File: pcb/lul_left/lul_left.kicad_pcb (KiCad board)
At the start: 2 copper layers, 238.5 x 84.2 mm, 48 parts, among them J1 JST Connector, J2 JST Connector, SW1 SW_Push, SW10 SW_Push, SW11 SW_Push, SW12 SW_Push, SW13 SW_Push, SW14 SW_Push, SW15 SW_Push, SW16 SW_Push, SW17 SW_Push, SW18 SW_Push, SW19 SW_Push, SW2 SW_Push, SW20 SW_Push, SW21 SW_Push, SW22 SW_Push, SW23 SW_Push, SW24 SW_Push, SW25 SW_Push, SW26 SW_Push, SW27 SW_Push, SW28 SW_Push, SW29 SW_Push, SW3 SW_Push, SW30 SW_Push, SW31 SW_Push, SW32 SW_Push, SW33 SW_Push, SW34 SW_Push, SW4 SW_Push, SW5 SW_Push, SW6 SW_Push, SW7 SW_Push, SW8 SW_Push, SW9 SW_Push, U1 nice_nano, U2 nice_nano

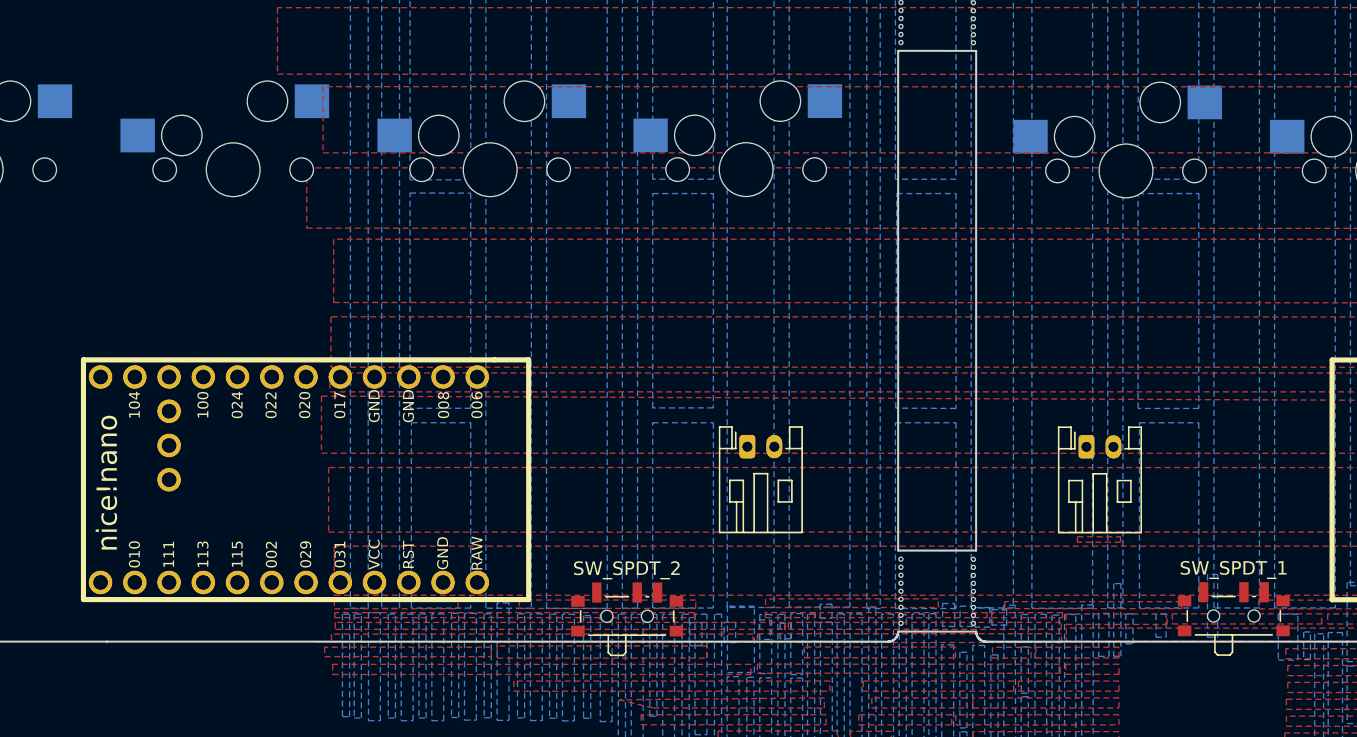
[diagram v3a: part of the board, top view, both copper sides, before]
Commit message: touch up dimensions and positions
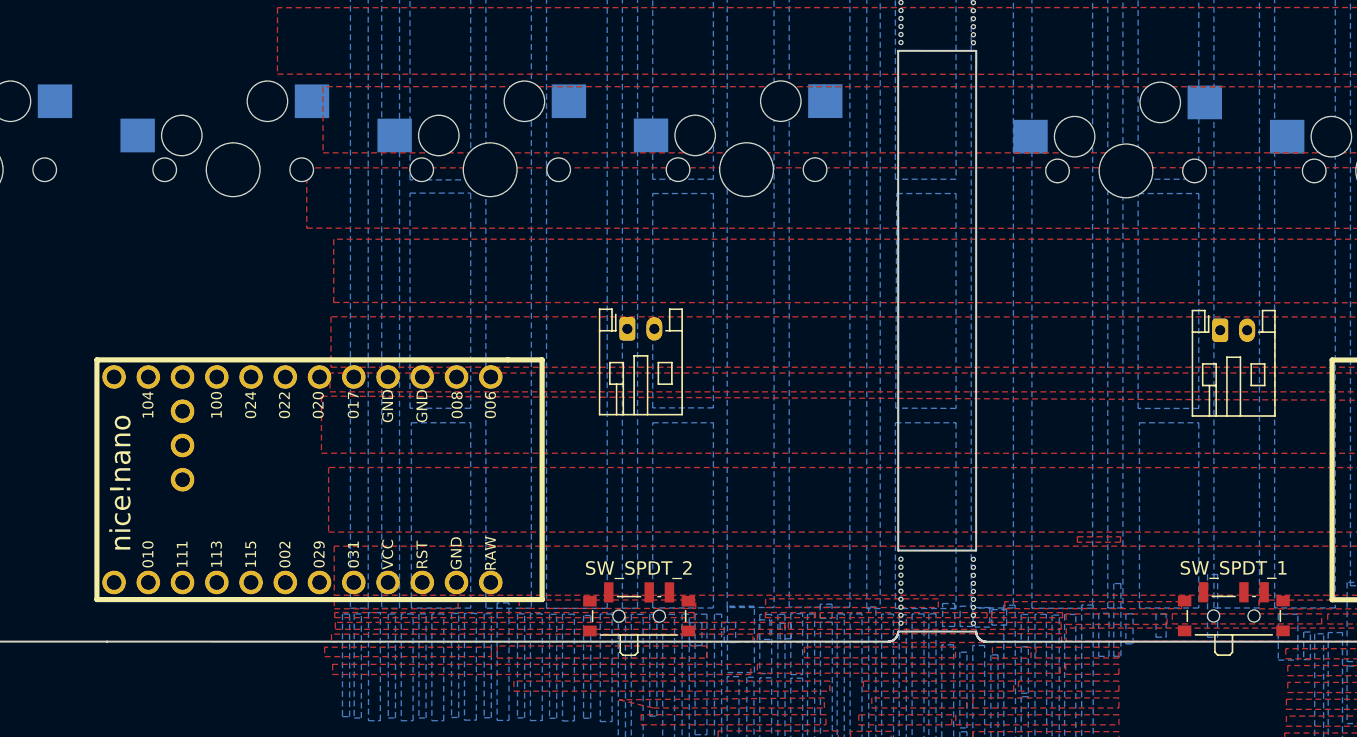
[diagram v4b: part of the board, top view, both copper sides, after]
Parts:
- moved J1 13.2 mm to (163.1, 83.2)
- moved J2 12.5 mm to (119.1, 83.1)
- moved U2 1.00 mm to (95.0, 94.3)
- moved SW_SPDT_2 0.89 mm to (120.0, 104.1)
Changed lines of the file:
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@@
   )
   (footprint "MX_Only:MXOnly-1U-Hotswap" (layer "F.Cu")
-    (at 127.929654 71.267042)
+    (at 127.96 71.27)
     (property "Sheetfile" "lul_left.kicad_sch")
     (property "Sheetname" "")
@@
   )
   (footprint "nice-nano-kicad:nice_nano" (layer "F.Cu")
-    (at 94.019654 94.267042 180)
+    (at 95.019654 94.267042 180)
     (property "Sheetfile" "lul_left.kicad_sch")
     (property "Sheetname" "")
@@
   )
   (footprint "Connector_JST:JST_PH_S2B-PH-K_1x02_P2.00mm_Horizontal" (layer "F.Cu")
-    (at 128.019654 91.817042)
+    (at 119.12 83.08)
     (descr "JST PH series connector, S2B-PH-K (http://www.jst-mfg.com/product/pdf/eng/ePH.pdf), generated with kicad-footprint-generator")
     (tags "connector JST PH top entry")
@@
   )
   (footprint "Button_Switch_SMD:SW_SPDT_PCM12" (layer "F.Cu")
-    (at 119.104654 104.067042)
+    (at 119.99 104.055)
     (descr "Ultraminiature Surface Mount Slide Switch, right-angle, https://www.ckswitches.com/media/1424/pcm.pdf")
     (property "Sheetfile" "lul_left.kicad_sch")
@@
   )
   (footprint "Connector_JST:JST_PH_S2B-PH-K_1x02_P2.00mm_Horizontal" (layer "F.Cu")
-    (at 153.17 91.83)
+    (at 163.09 83.18)
     (descr "JST PH series connector, S2B-PH-K (http://www.jst-mfg.com/product/pdf/eng/ePH.pdf), generated with kicad-footprint-generator")
     (tags "connector JST PH top entry")
@@
     (effects (font (size 1 0.9) (thickness 0.15)) (justify mirror))
   )
-  (gr_text "RIGHT" (at 20.57 162.46) (layer "Cmts.User")
+  (gr_text "RIGHT" (at 10 160.75) (layer "Cmts.User")
     (effects (font (size 30 30) (thickness 1)) (justify left bottom))
   )
-  (gr_text "LEFT" (at 166.44 163.02) (layer "Cmts.User")
+  (gr_text "LEFT" (at 184.93 158.88) (layer "Cmts.User")
     (effects (font (size 30 30) (thickness 1)) (justify left bottom))
   )
   (dimension (type aligned) (layer "Cmts.User")
-    (pts (xy 119.104654 104.067042) (xy 119.104654 106.287042))
-    (height 5.65)
-    (gr_text "2.2200 mm" (at 112.304654 105.177042 90) (layer "Cmts.User")
+    (pts (xy 119.99588 106.274313) (xy 120 104.05))
+    (height -6.373582)
+    (gr_text "2.22 mm" (at 112.474371 105.148221 89.89387364) (layer "Cmts.User")
       (effects (font (size 1 1) (thickness 0.15)))
     )
-    (format (prefix "") (suffix "") (units 3) (units_format 1) (precision 4))
+    (format (prefix "") (suffix "") (units 3) (units_format 1) (precision 4) (override_value "2.22"))
     (style (thickness 0.15) (arrow_length 1.27) (text_position_mode 0) (extension_height 0.58642) (extension_offset 0.5) keep_text_aligned)
   )
@@
   )
   (dimension (type aligned) (layer "Cmts.User")
+    (pts (xy 139.205015 105.52855) (xy 144.991563 105.531508))
+    (height 6.98262)
+    (gr_text "5.7865 mm" (at 142.095308 111.362648 359.9707112) (layer "Cmts.User")
+      (effects (font (size 1 1) (thickness 0.15)))
+    )
+    (format (prefix "") (suffix "") (units 3) (units_format 1) (precision 4))
+    (style (thickness 0.15) (arrow_length 1.27) (text_position_mode 0) (extension_height 0.58642) (extension_offset 0.5) keep_text_aligned)
+  )
+  (dimension (type aligned) (layer "Cmts.User")
+    (pts (xy 120.12 85.53) (xy 139.22 85.53))
+    (height 5.51)
+    (gr_text "19.1000 mm" (at 129.67 89.89) (layer "Cmts.User")
+      (effects (font (size 1 1) (thickness 0.15)))
+    )
+    (format (prefix "") (suffix "") (units 3) (units_format 1) (precision 4))
+    (style (thickness 0.15) (arrow_length 1.27) (text_position_mode 0) (extension_height 0.58642) (extension_offset 0.5) keep_text_aligned)
+  )
+  (dimension (type aligned) (layer "Cmts.User")
     (pts (xy 34.134654 79.577042) (xy 22.834654 79.567042))
     (height 6.363005)
@@
   )
   (dimension (type aligned) (layer "Cmts.User")
-    (pts (xy 119.099654 94.635577) (xy 94.019654 94.635577))
+    (pts (xy 120.12 85.53) (xy 120.12 80.8))
+    (height 6.41)
+    (gr_text "4.7300 mm" (at 128.23 81.98 90) (layer "Cmts.User")
+      (effects (font (size 1 1) (thickness 0.15)))
+    )
+    (format (prefix "") (suffix "") (units 3) (units_format 1) (precision 4))
+    (style (thickness 0.15) (arrow_length 1.27) (text_position_mode 2) (extension_height 0.58642) (extension_offset 0.5) keep_text_aligned)
+  )
+  (dimension (type aligned) (layer "Cmts.User")
+    (pts (xy 164.09 85.63) (xy 164.089451 80.9))
+    (height -6.0957)
+    (gr_text "4.7300 mm" (at 156.229451 83.58 -89.9933377) (layer "Cmts.User")
+      (effects (font (size 1 1) (thickness 0.15)))
+    )
+    (format (prefix "") (suffix "") (units 3) (units_format 1) (precision 4))
+    (style (thickness 0.15) (arrow_length 1.27) (text_position_mode 2) (extension_height 0.58642) (extension_offset 0.5) keep_text_aligned)
+  )
+  (dimension (type aligned) (layer "Cmts.User")
+    (pts (xy 164.09 85.63) (xy 144.989451 85.63))
+    (height -5.24)
+    (gr_text "19.1005 mm" (at 154.539725 89.72) (layer "Cmts.User")
+      (effects (font (size 1 1) (thickness 0.15)))
+    )
+    (format (prefix "") (suffix "") (units 3) (units_format 1) (precision 4))
+    (style (thickness 0.15) (arrow_length 1.27) (text_position_mode 0) (extension_height 0.58642) (extension_offset 0.5) keep_text_aligned)
+  )
+  (dimension (type aligned) (layer "Cmts.User")
+    (pts (xy 119.98 94.26) (xy 95.019654 94.267042))
     (height -17.921465)
-    (gr_text "25.0 mm" (at 106.559654 111.407042) (layer "Cmts.User")
+    (gr_text "25.0 mm" (at 107.504559 111.034985 0.01616471457) (layer "Cmts.User")
       (effects (font (size 1 1) (thickness 0.15)))
     )
@@
   )
   (dimension (type aligned) (layer "Cmts.User")
-    (pts (xy 94.019654 94.267042) (xy 61.019654 94.267042))
+    (pts (xy 95.019654 94.267042) (xy 61.019654 94.267042))
     (height -18.29)
-    (gr_text "33.0000 mm" (at 77.519654 111.407042) (layer "Cmts.User")
+    (gr_text "34.0000 mm" (at 78.019654 111.407042) (layer "Cmts.User")
       (effects (font (size 1 1) (thickness 0.15)))
     )

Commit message: route switches nicely
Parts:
- removed the REF** at (139.4, 59.5)
- removed the REF** at (144.8, 25.9)
- removed the REF** at (139.4, 102.5)
- removed the REF** at (139.4, 25.9)
- removed the REF** at (144.8, 59.5)
- removed the REF** at (144.8, 102.5)
- added REF**: Hole_Breakaway-Tabs, zzkeeb:Hole_Breakaway-Tabs, F.Cu at (139.4, 25.9)
- added REF**: Hole_Breakaway-Tabs, zzkeeb:Hole_Breakaway-Tabs, F.Cu at (144.8, 25.9)
- added REF**: Hole_Breakaway-Tabs, zzkeeb:Hole_Breakaway-Tabs, F.Cu at (144.8, 59.4)
- added REF**: Hole_Breakaway-Tabs, zzkeeb:Hole_Breakaway-Tabs, F.Cu at (139.4, 59.4)
- added REF**: Hole_Breakaway-Tabs, zzkeeb:Hole_Breakaway-Tabs, F.Cu at (139.4, 102.5)
- added REF**: Hole_Breakaway-Tabs, zzkeeb:Hole_Breakaway-Tabs, F.Cu at (144.8, 102.5)
- moved SW_RESET2 97.2 mm to (131.1, 85.5)
- moved SW_RESET_1 97.2 mm to (153.1, 85.6)
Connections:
- U2 pad 1: R9 -> R3
- U2 pad 10: R15 -> R13
- U2 pad 11: R16 -> R10
- U2 pad 12: R17 -> R6
- U2 pad 13: R8 -> R4
- U2 pad 14: R7 -> R8
- U2 pad 15: R6 -> R1
- U2 pad 17: R4 -> R9
- U2 pad 18: R3 -> R12
- U2 pad 19: R2 -> R15
- U2 pad 20: R1 -> R2
- U2 pad 5: R10 -> R7
- U2 pad 7: R12 -> R16
- U2 pad 8: R13 -> R6
- U2 pad 9: R14 -> R16
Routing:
- net R15: track 0.00 -> 199.7 mm
- net R12: track 0.00 -> 179.2 mm
- net R9: track 0.00 -> 158.4 mm
- net R16: track 0.00 -> 157.5 mm
- net R17: track 0.00 -> 156.3 mm
- net R14: track 0.00 -> 138.1 mm
- net R5: track 0.00 -> 137.5 mm
- net R13: track 0.00 -> 136.9 mm
- net R11: track 0.00 -> 119.8 mm
- net R1: track 0.00 -> 117.1 mm
- net R10: track 0.00 -> 116.1 mm
- net R2: track 0.00 -> 107.5 mm
- net R7: track 0.00 -> 101.8 mm
- net R6: track 0.00 -> 95.6 mm
- net R3: track 0.00 -> 79.5 mm
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
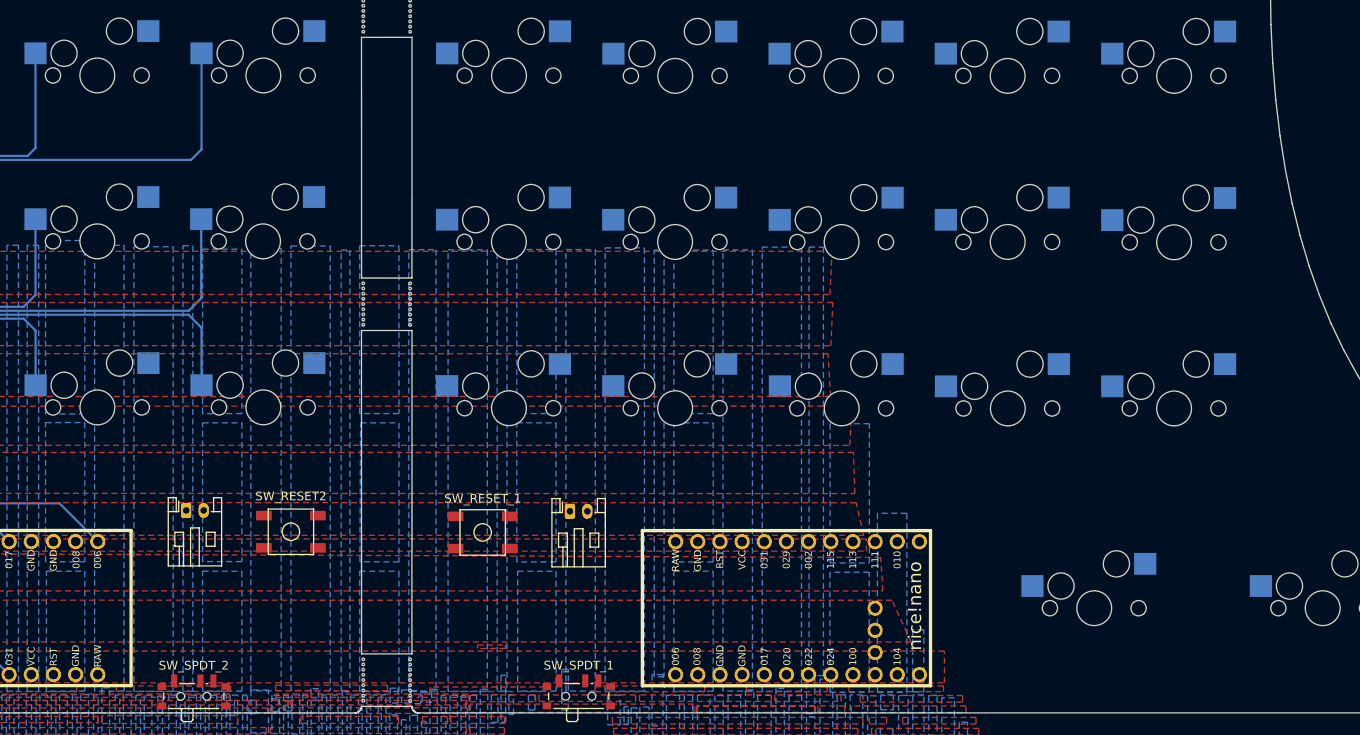
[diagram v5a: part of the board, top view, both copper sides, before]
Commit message: route fully. Just need ground fill
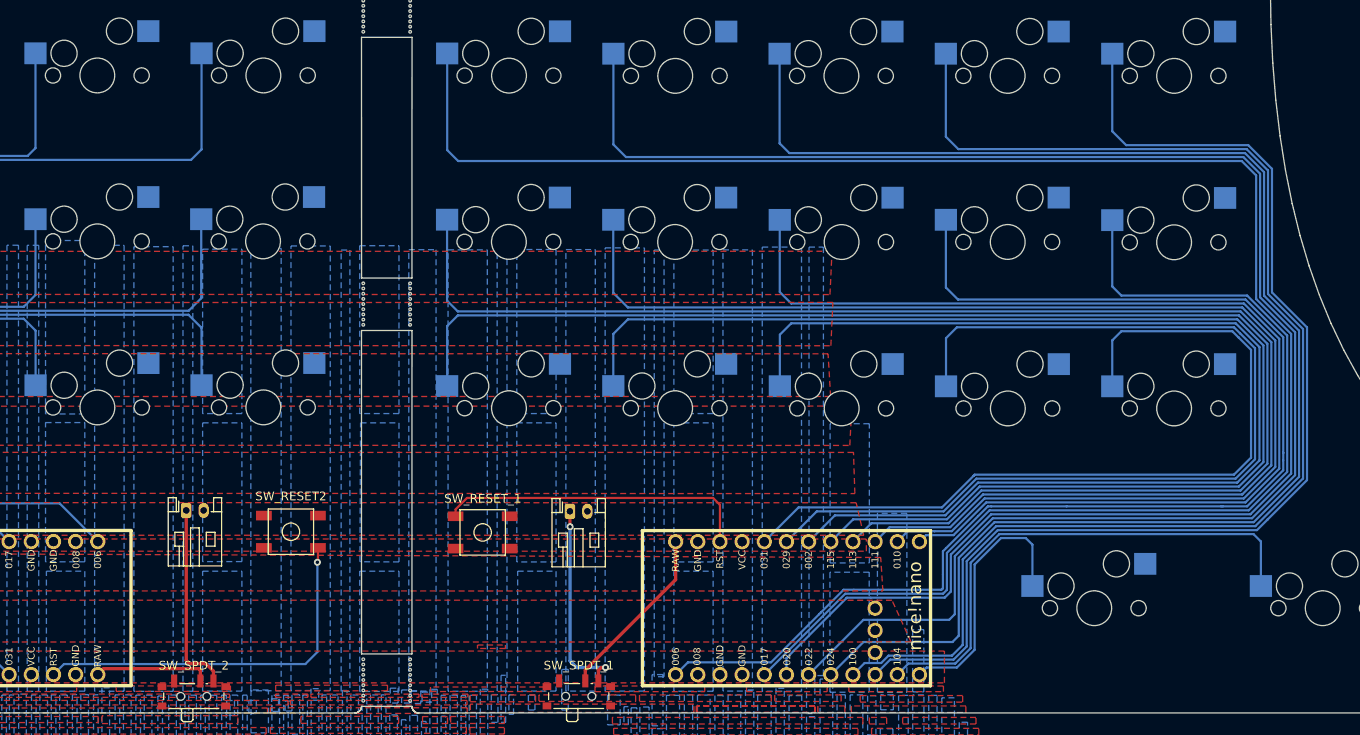
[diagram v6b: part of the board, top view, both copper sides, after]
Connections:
- U1 pad 1: L1 -> L11
- U1 pad 10: L7 -> L14
- U1 pad 11: L8 -> L17
- U1 pad 12: L9 -> L13
- U1 pad 13: L17 -> L8
- U1 pad 14: L16 -> L5
- U1 pad 15: L15 -> L2
- U1 pad 16: L14 -> L3
- U1 pad 17: L13 -> L6
- U1 pad 18: L12 -> L9
- U1 pad 19: L11 -> L12
- U1 pad 20: L10 -> L16
- U1 pad 21: VCC -> unconnected-(U1-VCC-Pad21)
- U1 pad 5: L2 -> L15
- U1 pad 6: L3 -> L1
- U1 pad 8: L5 -> L7
- U1 pad 9: L6 -> L10
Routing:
- net L1: track 0.00 -> 211.7 mm
- net L4: track 0.00 -> 191.2 mm
- net L7: track 0.00 -> 172.0 mm
- net L2: track 0.00 -> 168.8 mm
- net L3: track 0.00 -> 167.6 mm
- net L10: track 0.00 -> 151.6 mm
- net L6: track 0.00 -> 149.1 mm
- net L5: track 0.00 -> 147.9 mm
- net L11: track 0.00 -> 145.9 mm
- net L9: track 0.00 -> 131.0 mm
- net L14: track 0.00 -> 130.8 mm
- net L8: track 0.00 -> 127.3 mm
- net L15: track 0.00 -> 117.6 mm
- net L12: track 0.00 -> 112.8 mm
- net L16: track 0.00 -> 94.6 mm
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
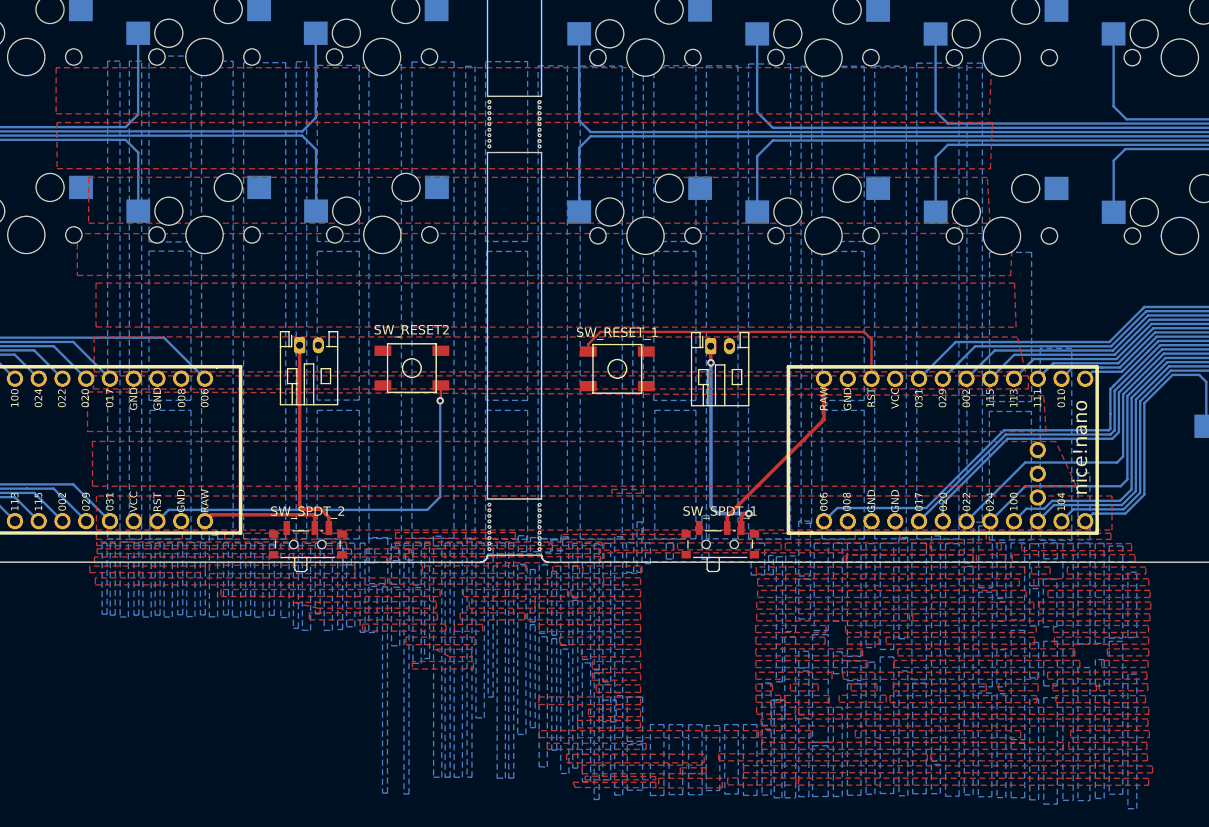
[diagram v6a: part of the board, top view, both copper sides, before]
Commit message: remove the old fill zones
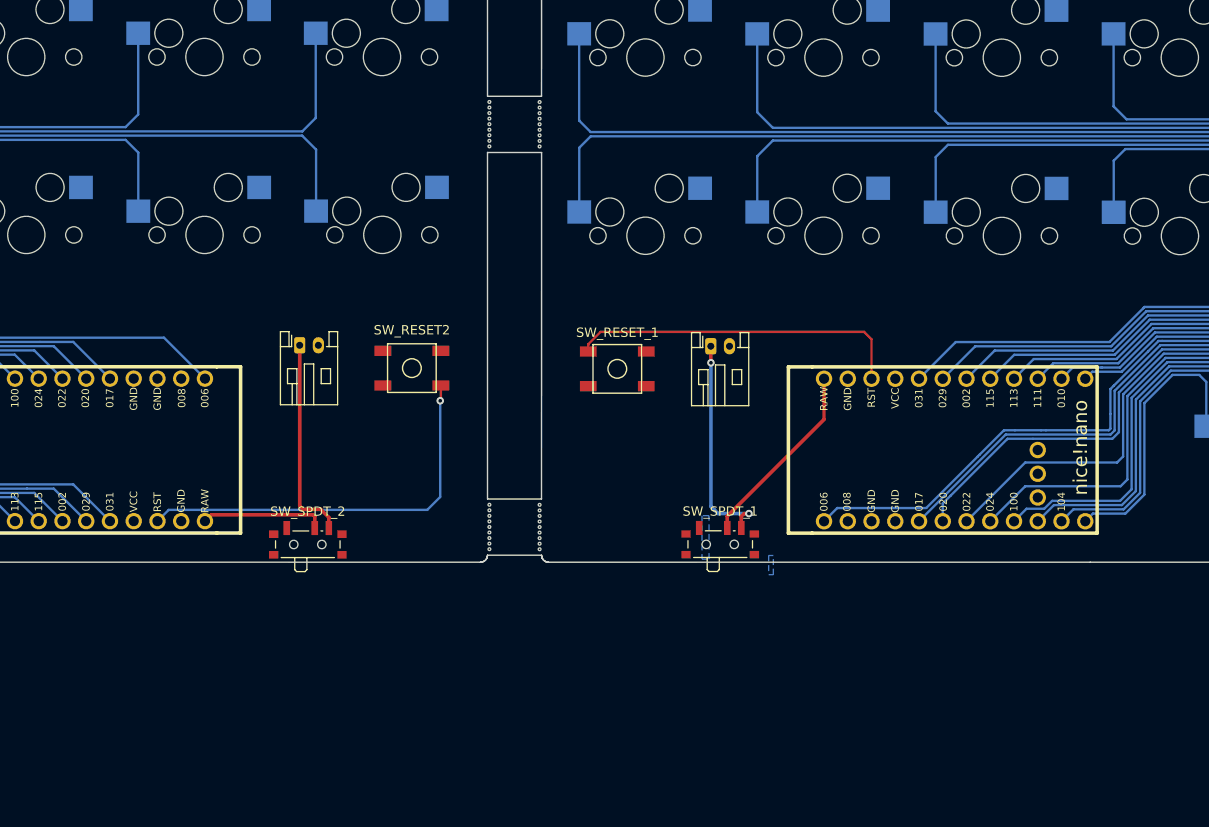
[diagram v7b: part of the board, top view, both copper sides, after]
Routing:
- removed copper zone on F.Cu, net (none)
- removed copper zone on B.Cu, net GND
- removed copper zone on F.Cu, net GND
- removed copper zone on B.Cu, net L12
- removed copper zone on F.Cu, net L12
- removed copper zone on B.Cu, net L13
- removed copper zone on F.Cu, net L13
- removed copper zone on F.Cu, net L14
- removed copper zone on B.Cu, net L17
- removed copper zone on F.Cu, net L17
- removed copper zone on B.Cu, net L4
- removed copper zone on F.Cu, net L4
- removed copper zone on B.Cu, net L5
- removed copper zone on F.Cu, net L5
- removed copper zone on B.Cu, net L6
- removed copper zone on F.Cu, net L6
- removed copper zone on B.Cu, net L7
- removed copper zone on F.Cu, net L7
